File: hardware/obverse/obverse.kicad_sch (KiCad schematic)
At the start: 33 parts, among them J1 Conn_01x04, J2 Conn_01x03, U1 WCH CH32V003F4U6

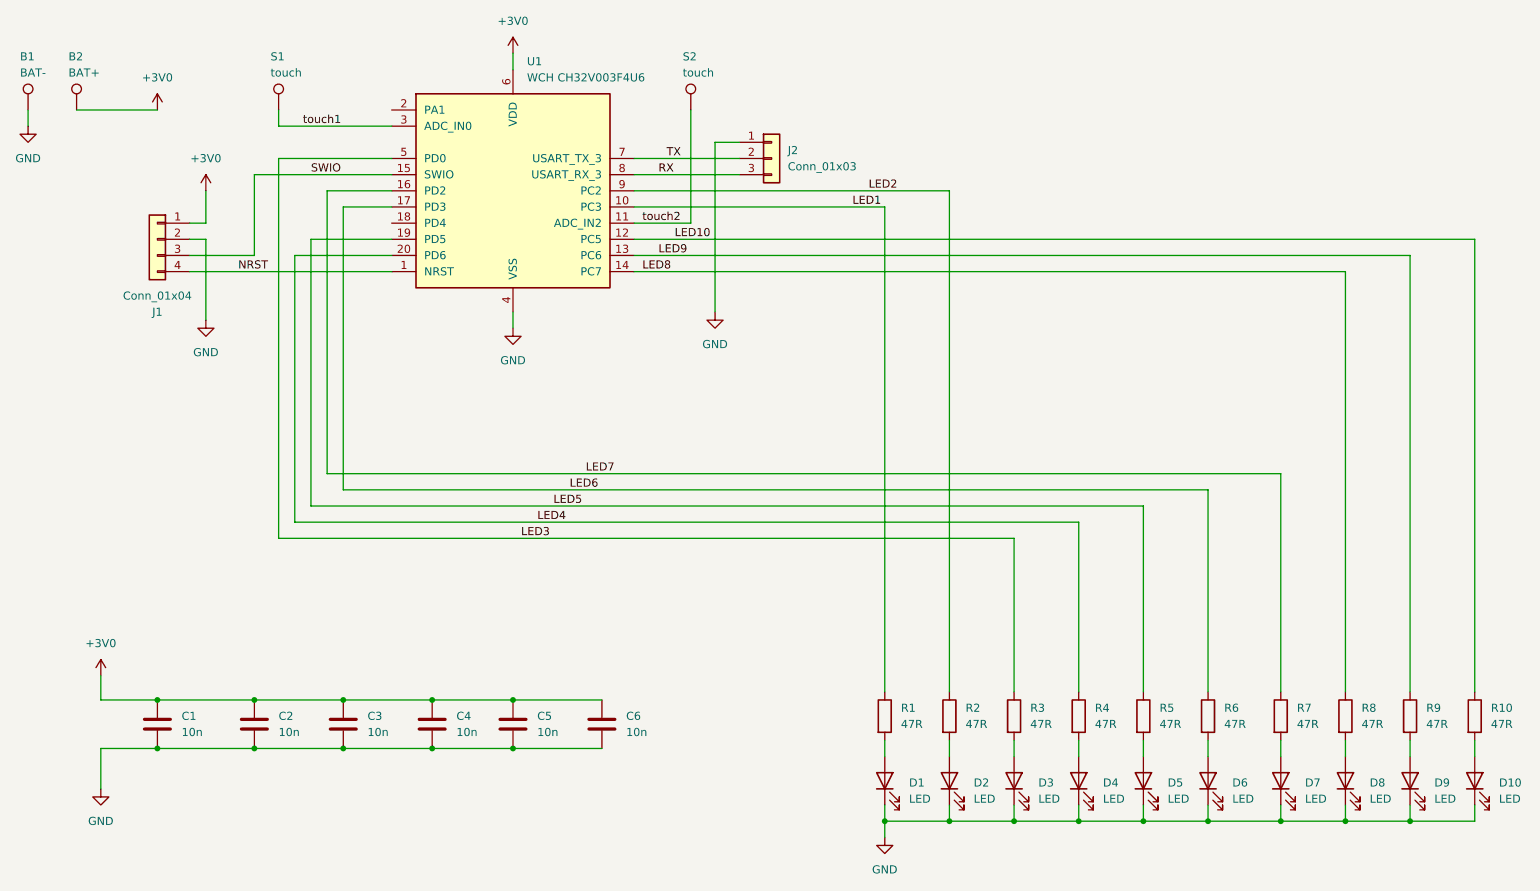
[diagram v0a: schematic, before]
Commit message: separate boards and generate fab files
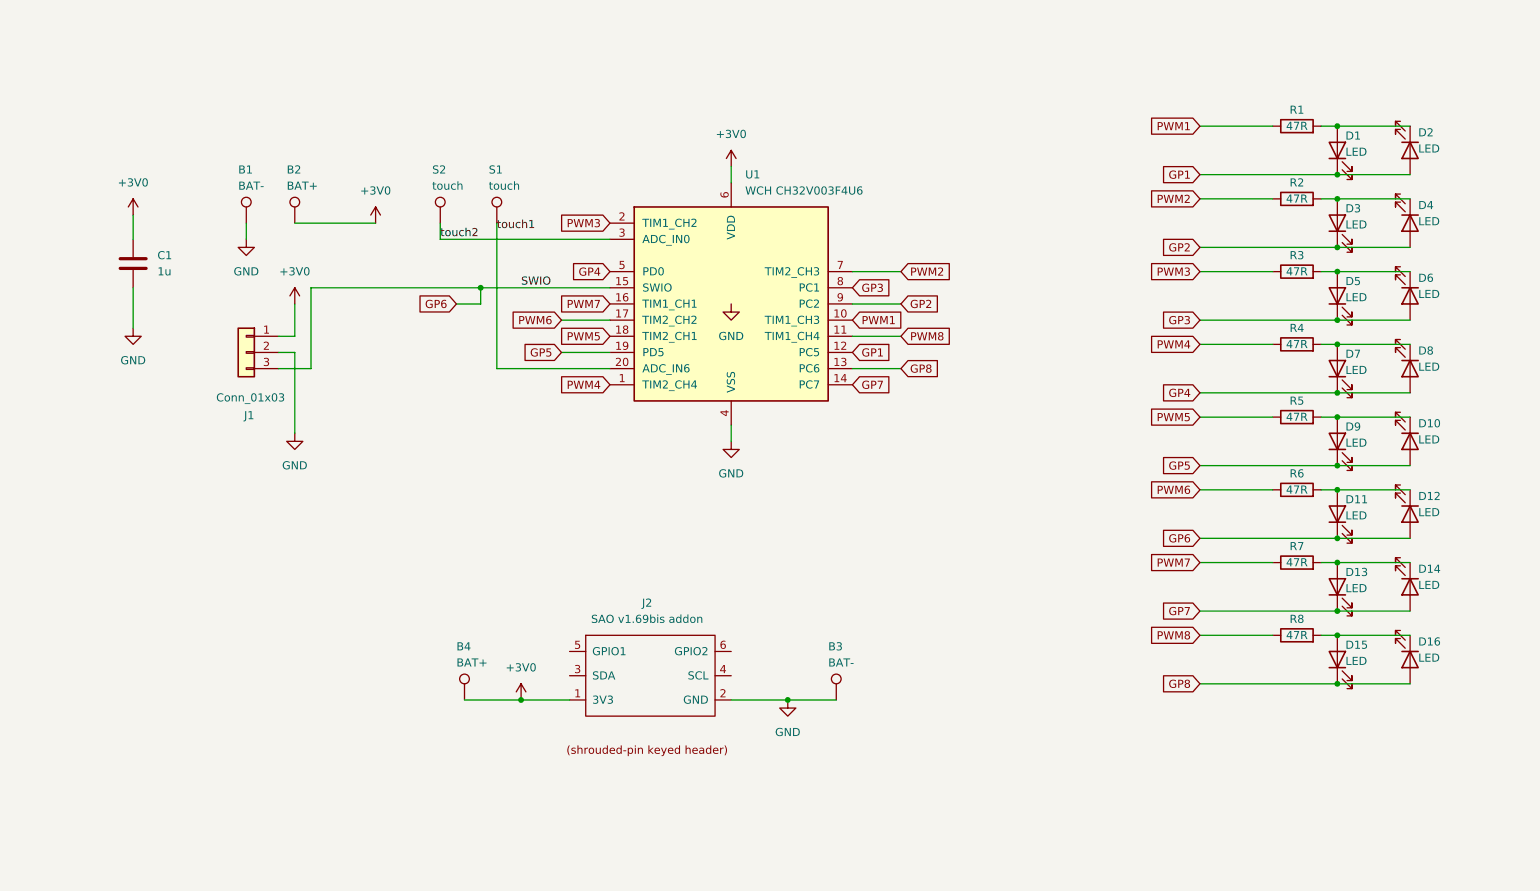
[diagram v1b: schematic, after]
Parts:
- removed C2, C3, C4, C5, C6: 10n, Capacitor_SMD:C_0402_1005Metric, symbol Device:C
- removed J1: Conn_01x04, Connector_PinHeader_1.27mm:PinHeader_1x04_P1.27mm_Vertical, symbol Connector_Generic:Conn_01x04
- removed J2: Conn_01x03, Connector_PinHeader_1.27mm:PinHeader_1x03_P1.27mm_Vertical, symbol Connector_Generic:Conn_01x03
- removed R10, R9: 47R, Resistor_SMD:R_0402_1005Metric, symbol Device:R
- added B3: BAT-, TestPoint:TestPoint_Pad_D4.0mm, symbol Connector:TestPoint
- added B4: BAT+, TestPoint:TestPoint_Pad_D4.0mm, symbol Connector:TestPoint
- added D11, D12, D13, D14, D15, D16: LED, LED_SMD:LED_0402_1005Metric, symbol Device:LED
- added J1: Conn_01x03, Connector_PinHeader_1.27mm:PinHeader_1x03_P1.27mm_Vertical, symbol Connector_Generic:Conn_01x03
- added J2: SAO v1.69bis addon, Connector_IDC:IDC-Header_2x03_P2.54mm_Vertical, symbol extra:SAO v1.69bis addon
- C1: value 10n -> 1u; LCSC C696856 -> C7393851
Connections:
- net LED10 is gone; now on net GP1: U1.12 (PC5)
- net NRST is gone; now on net PWM4: U1.1 (PD7)
- net VSS is gone; now on net GND: U1.21 (VSS)
- net +3V0: now also B4.1, J1.1 (Pin_1), J2.1 (3V3)
- net GND: now also B3.1, J1.2 (Pin_2), J2.2 (GND); no longer D1.1 (K), D10.1 (K), D2.1 (K), D3.1 (K), D4.1 (K), D5.1 (K), D6.1 (K), D7.1 (K), D8.1 (K), D9.1 (K)
- net touch1: now also U1.20 (PD6); no longer U1.3 (PA2)
- net touch2: now also U1.3 (PA2); no longer U1.11 (PC4)
- net at R4.2: now also D7.2 (A), D8.1 (K); no longer D4.2 (A)
- net at D3.2 (A): now also D4.1 (K), R2.2; no longer R3.2
- net at D9.2 (A): now also D10.1 (K), R5.2
- net at R6.2: now also D11.2 (A), D12.1 (K); no longer D6.2 (A)
- net GP5: now reaches D10.2 (A)
- net GP5: now also D9.1 (K), U1.19 (PD5)
- net at R8.2: now also D15.2 (A), D16.1 (K); no longer D8.2 (A)
- net at R7.2: now also D13.2 (A), D14.1 (K); no longer D7.2 (A)
- net at D1.2 (A), R1.2: now also D2.1 (K)
- net at D5.2 (A): now also D6.1 (K), R3.2; no longer R5.2
- net GP1: now reaches D2.2 (A)
- net GP1: now also D1.1 (K); no longer R2.2
- net PWM5: now reaches U1.18 (PD4)
- net PWM5: now also R5.1
- net PWM3: now reaches U1.2 (PA1)
- net PWM3: now also R3.1
- net LED1 renamed PWM1
- net LED2 renamed GP2
- net GP2: now also D3.1 (K), D4.2 (A); no longer R2.1
- net LED3 renamed GP4
- net GP4: now also D7.1 (K), D8.2 (A); no longer R3.1
- net LED4 renamed PWM4
- net PWM4: no longer U1.20 (PD6)
- removed net LED5: R5.1, U1.19 (PD5)
- net LED6 renamed PWM6
- net LED7 renamed PWM7
- net LED8 renamed GP7
- net GP7: now also D13.1 (K), D14.2 (A); no longer R8.1
- net LED9 renamed GP8
- net GP8: now also D15.1 (K), D16.2 (A)
- net RX renamed GP3
- net GP3: now also D5.1 (K), D6.2 (A)
- net SWIO renamed GP6
- net GP6: now also D11.1 (K), D12.2 (A), J1.3 (Pin_3)
- net TX renamed PWM2
- net PWM2: now also R2.1
- new net PWM8: R8.1, U1.11 (PC4)
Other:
- moved on the sheet: B1, B2, D10, D2, D3, D4, D5, D6, D7, D8, D9, S1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
